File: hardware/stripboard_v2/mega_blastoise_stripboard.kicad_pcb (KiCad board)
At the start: 2 copper layers, 61 x 142.2 mm, 26 parts, among them J1 PinHeader_1x08_P2.54mm_Vertic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, J2 PinHeader_1x02_P2.54mm_Vertic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, J3 PinHeader_1x02_P2.54mm_Vertic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, SW17 PinHeader_1x02_P2.54mm_Vertic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, U1 RaspberryPi_Pico_Common_THT

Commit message: Move the battery divider north so its sense wire clears the Pico
All three ADC pins are on the Pico's north pin row, so the sense wire has
to terminate above the row-30 cut no matter what. With the divider south
of the Pico that meant a wire running I24 to V37, 64 percent of which lay
underneath the module: legal, but the one wire that could never be
inspected or reworked once the Pico was down.

R1, R2 and C1 move to rows 22-28 on columns T, V and X. That works
because VBATT_SW lives on column X rows 23-36, which spans the Pico rows
uninterrupted, and column T's north segment carries Pico pin 23, a ground
pin. The sense wire becomes I13 to V13: 33 mm, entirely clear of the
module, and the V column no longer needs its row-35 cut.

Wire drops 368 mm to 354 mm and cuts 43 to 42.

verify.py gained a way to read the passives correctly. R1, R2 and C1 have
no polarity, so which lead is pad 1 says nothing about which net it is on;
the net follows the column the lead lands in. Reading them by pad number
reported six phantom shorts on a board that was fine.

Co-Authored-By: Claude Opus 5 <noreply@anthropic.com>
Claude-Session: https://claude.ai/code/session_01DtJPckCX3BS4baXMVDqKJx
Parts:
- moved C1 50.8 mm to (74.6, 74.6)
- moved R2 40.6 mm to (74.6, 79.7)
- moved R1 20.3 mm to (79.7, 89.8)
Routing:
- net (no net): track 3502.1 -> 3493.5 mm

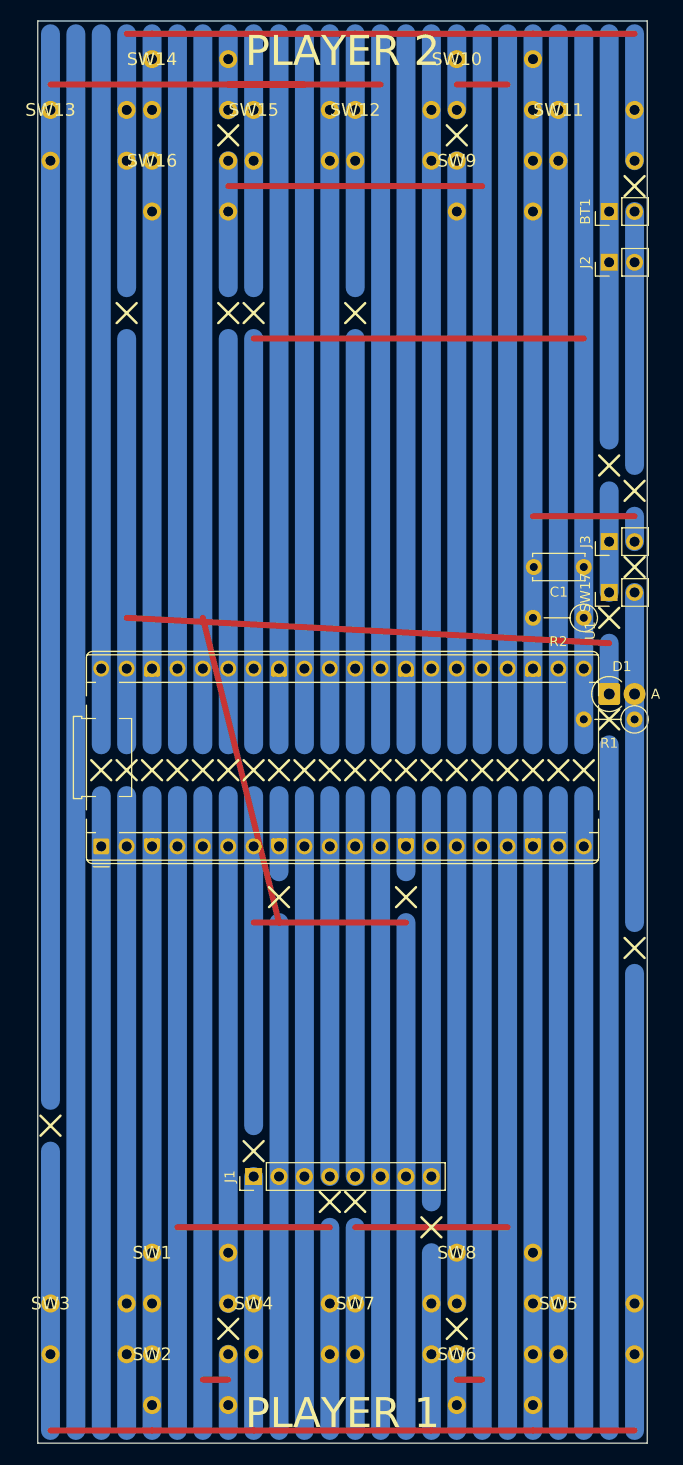
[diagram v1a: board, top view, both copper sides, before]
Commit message: Drop the Pico four rows so the power tail is not under it
R1's V-column lead sat inside the Pico's body footprint and D1 was hard
against its right edge, which meant two parts of the power tail could not
be reached once the module was soldered down. Moving the Pico from rows
26/33 to 30/37 (cut row 34) puts the whole tail above it: R1 clears by
3.5 mm, D1 by 6 mm, and everything else on W and X by more.

Two fences, J35 and O35, ended up between the new pin rows and moved to
39, below the module. Every wire hint was re-anchored to a pad rather
than a row, since after a move like this a stored row number no longer
names the segment it used to; the router then picked its own endpoints.

Wire length and cut count are unchanged at 354 mm and 42. The board is
otherwise the same: same pin map, same nets, same 26 parts.

Co-Authored-By: Claude Opus 5 <noreply@anthropic.com>
Claude-Session: https://claude.ai/code/session_01DtJPckCX3BS4baXMVDqKJx
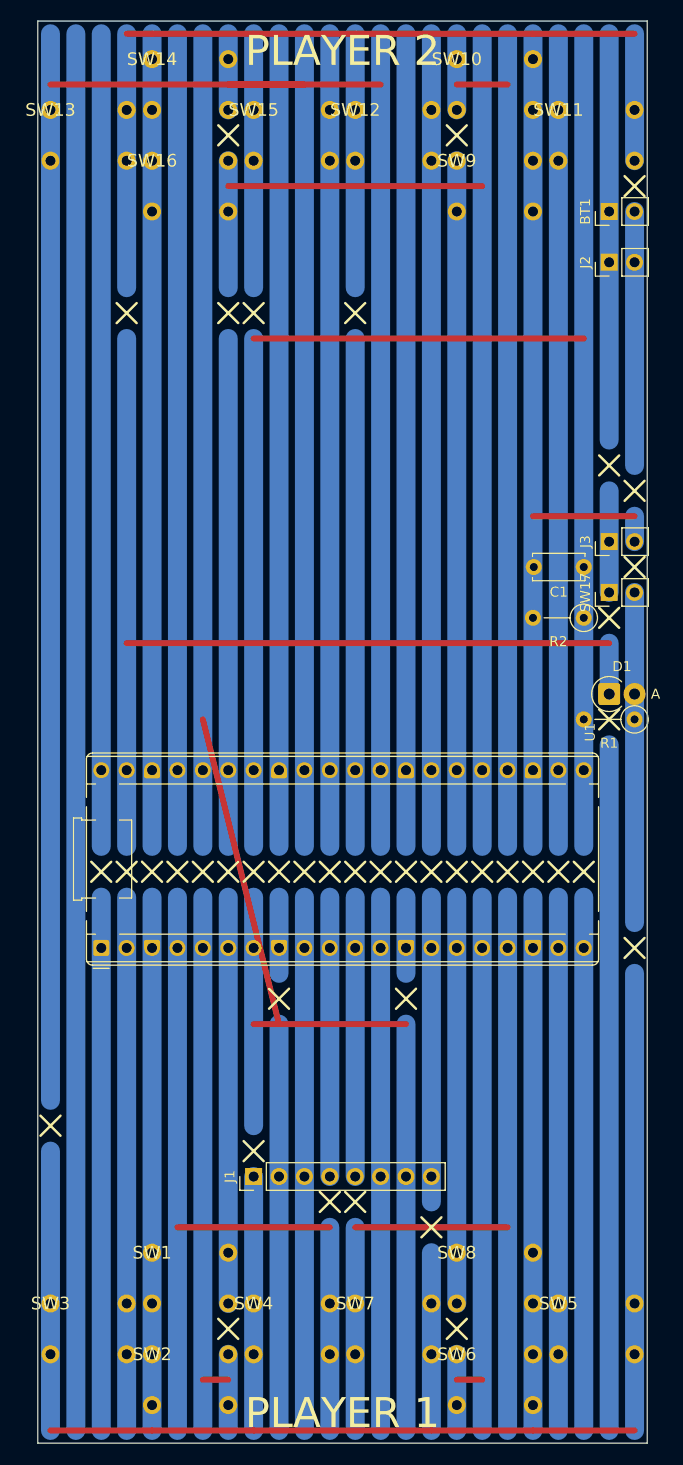
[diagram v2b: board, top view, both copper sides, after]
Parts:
- moved U1 10.2 mm to (26.4, 112.7)

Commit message: Keep GP16 off the battery sense tap
Column V carries both the divider tap and, at the Pico's upper pin row,
GP16. They were the same conductor, so GP16 sat directly on the node GP28
is trying to measure. Nothing would have been damaged, but firmware
driving GP16 as an output would have silently pinned the gauge to 3V3 or
to zero, and GP16 is listed as free for exactly that kind of use.

A cut at V28 separates them. R1 moves up two rows to V26/X26 so the cut
can sit two rows clear of the pin row, which is the rule the rest of the
fences follow.

Found while answering whether the charging caveat needed a rework. It did
not; this did.

Co-Authored-By: Claude Opus 5 <noreply@anthropic.com>
Claude-Session: https://claude.ai/code/session_01DtJPckCX3BS4baXMVDqKJx
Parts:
- moved R1 5.08 mm to (79.7, 84.8)
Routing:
- net (no net): track 3493.4 -> 3488.4 mm
